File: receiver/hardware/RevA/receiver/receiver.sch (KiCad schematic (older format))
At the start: 1 part, among them U1 C8051F850-A-GU

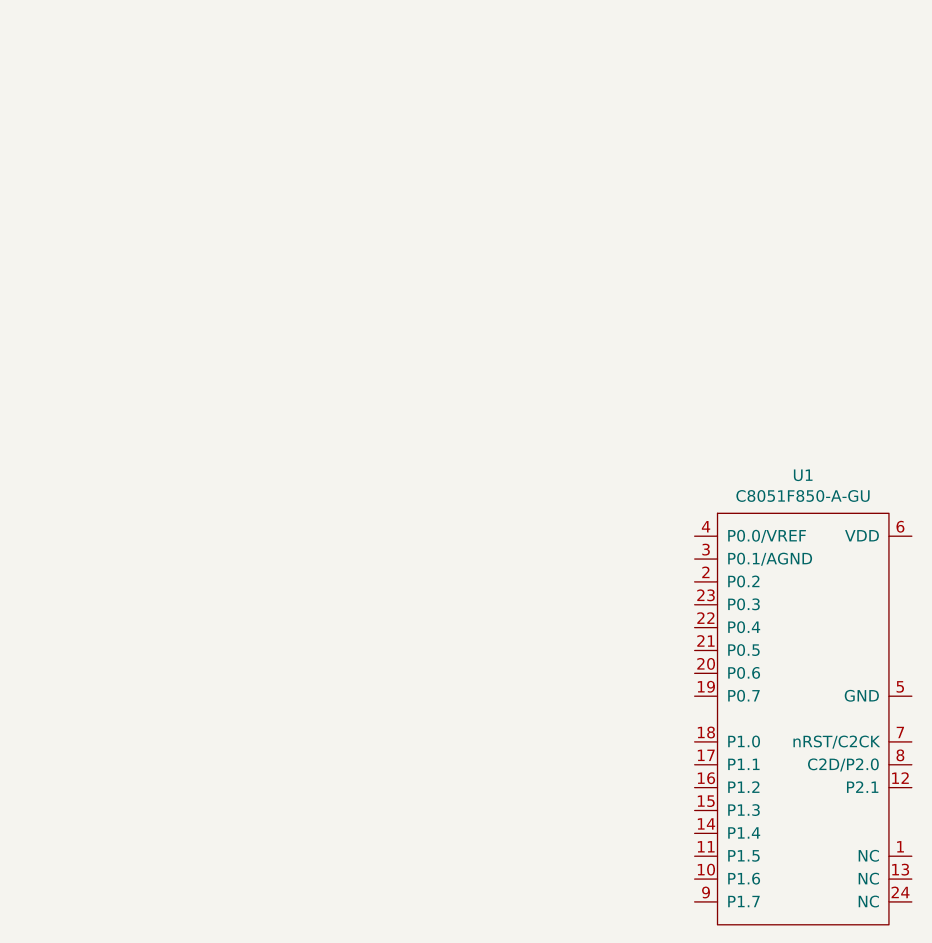
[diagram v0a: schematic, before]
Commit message: Added FT232RL
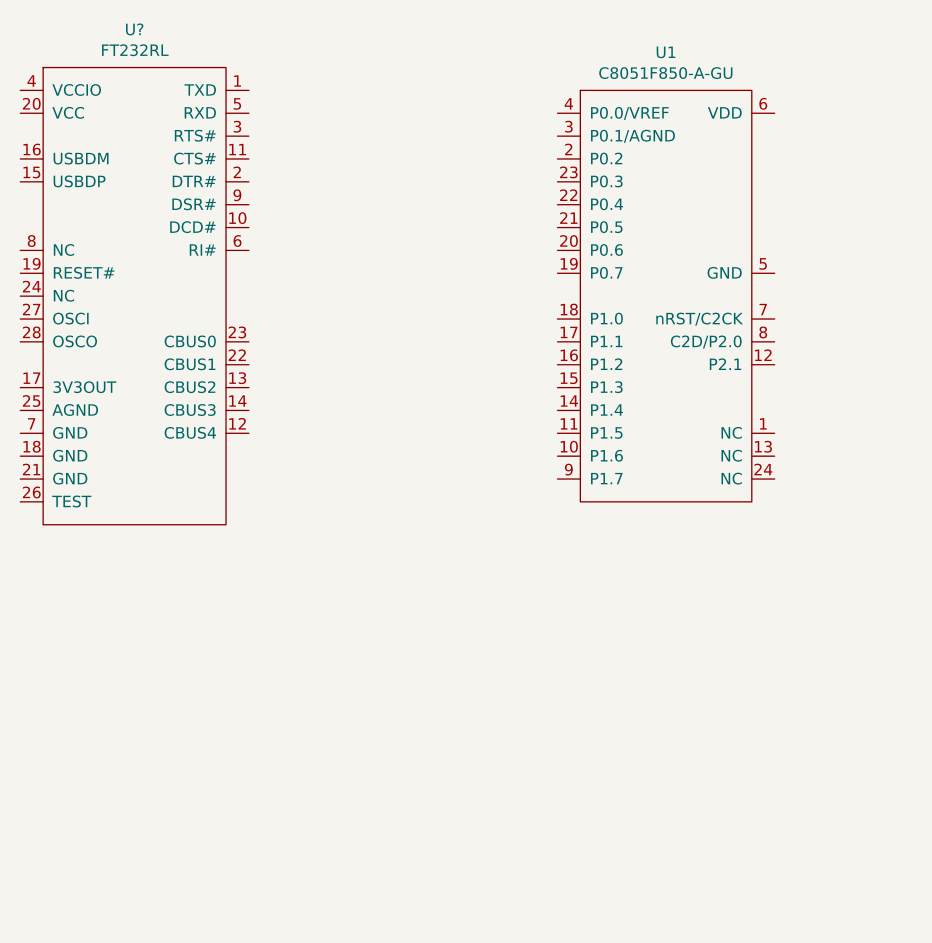
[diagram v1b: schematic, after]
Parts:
- added U?: FT232RL, symbol receiver:FT232RL
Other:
- moved on the sheet: U1
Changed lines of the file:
@@
 L receiver:C8051F850-A-GU U1
 U 1 1 61B9295A
-P 4550 4200
-F 0 "U1" H 5075 4365 50  0000 C CNN
-F 1 "C8051F850-A-GU" H 5075 4274 50  0000 C CNN
-F 2 "receiver:C8051F850-A-GU" H 4600 4100 50  0001 C CNN
-F 3 "" H 4600 4100 50  0001 C CNN
-	1    4550 4200
+P 3950 2350
+F 0 "U1" H 4475 2515 50  0000 C CNN
+F 1 "C8051F850-A-GU" H 4475 2424 50  0000 C CNN
+F 2 "receiver:C8051F850-A-GU" H 4000 2250 50  0001 C CNN
+F 3 "" H 4000 2250 50  0001 C CNN
+	1    3950 2350
 	1    0    0    -1
 $EndComp
+$Comp
+L receiver:FT232RL U?
+U 1 1 61BC06A2
+P 2650 2350
+F 0 "U?" H 2150 2615 50  0000 C CNN
+F 1 "FT232RL" H 2150 2524 50  0000 C CNN
+F 2 "" H 2650 2350 50  0001 C CNN
+F 3 "" H 2650 2350 50  0001 C CNN
+	1    2650 2350
+	1    0    0    -1
+$EndComp

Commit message: ftdi and usb
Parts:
- added J1: 48037-0001, receiver:48037-0001, symbol receiver:48037-0001
- U2: renamed from U?; footprint (none) -> receiver:FT232RL
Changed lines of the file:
@@
 $EndComp
 $Comp
-L receiver:FT232RL U?
+L receiver:FT232RL U2
 U 1 1 61BC06A2
 P 2650 2350
-F 0 "U?" H 2150 2615 50  0000 C CNN
+F 0 "U2" H 2150 2615 50  0000 C CNN
 F 1 "FT232RL" H 2150 2524 50  0000 C CNN
-F 2 "" H 2650 2350 50  0001 C CNN
+F 2 "receiver:FT232RL" H 2650 2350 50  0001 C CNN
 F 3 "" H 2650 2350 50  0001 C CNN
 	1    2650 2350
 	1    0    0    -1
 $EndComp
+$Comp
+L receiver:48037-0001 J1
+U 1 1 61BD1ABB
+P 900 2500
+F 0 "J1" H 858 2765 50  0000 C CNN
+F 1 "48037-0001" H 858 2674 50  0000 C CNN
+F 2 "receiver:48037-0001" H 900 2500 50  0001 C CNN
+F 3 "" H 900 2500 50  0001 C CNN
+	1    900  2500
+	1    0    0    -1
+$EndComp

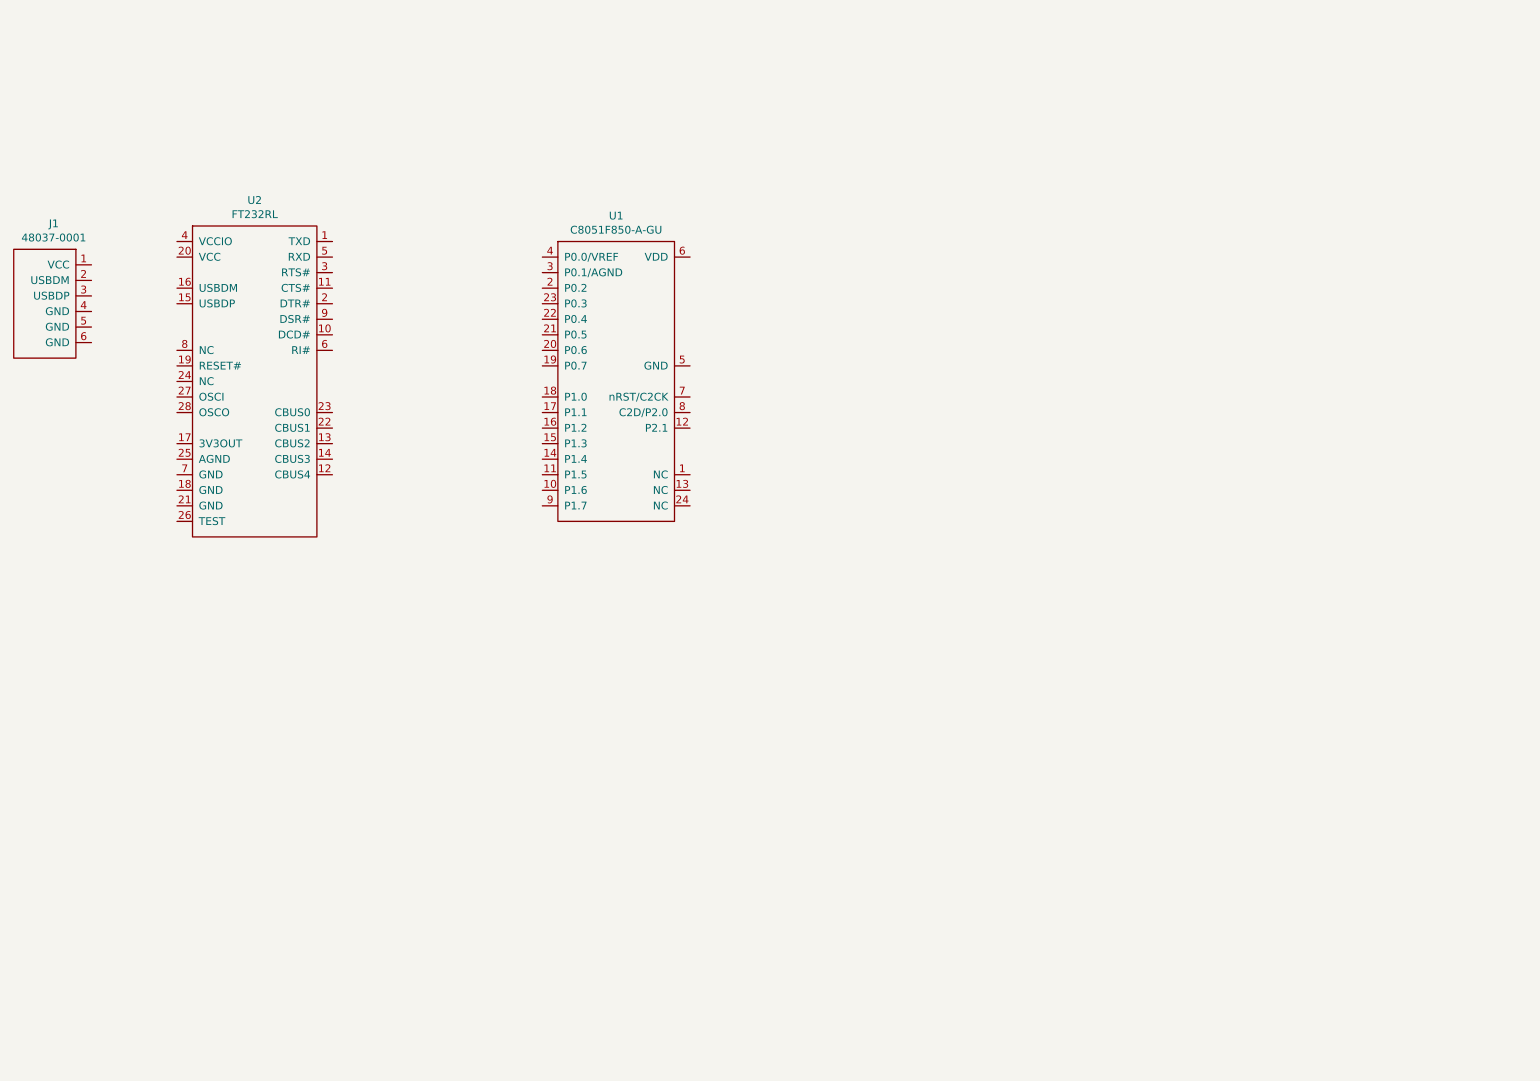
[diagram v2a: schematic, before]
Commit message: add connector
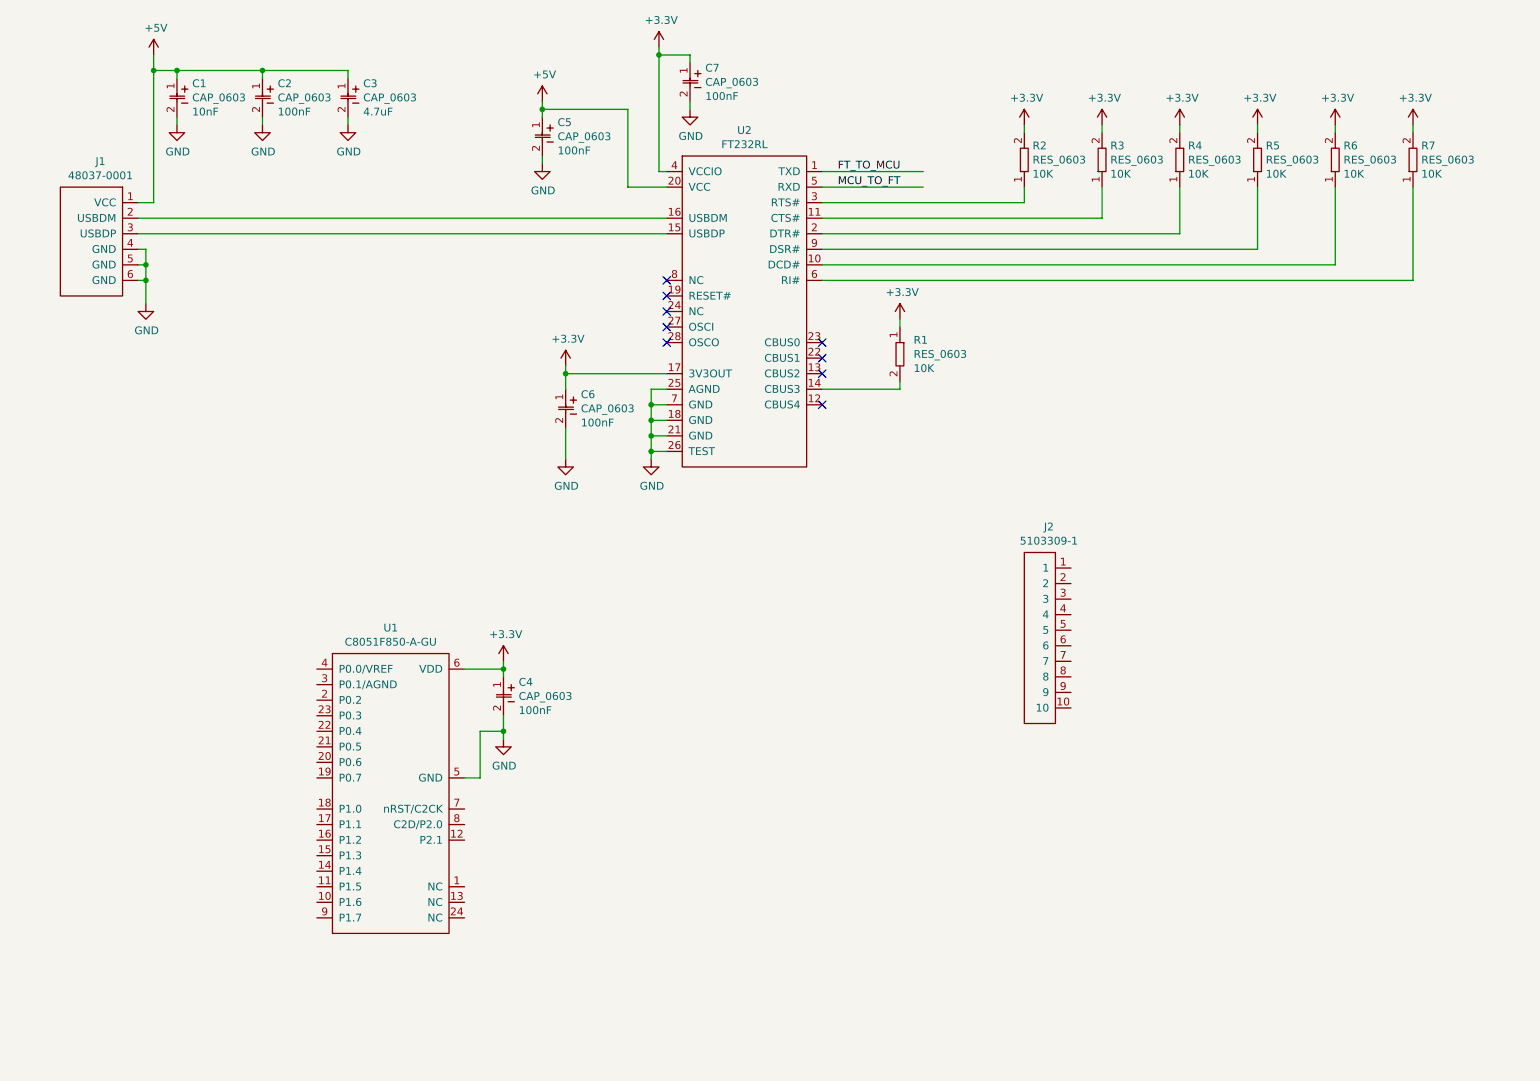
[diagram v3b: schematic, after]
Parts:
- added C1, C2, C3, C4, C5, C6, C7: CAP_0603, receiver:0603, symbol receiver:CAP_0603
- added J2: 5103309-1, receiver:5103309-1, symbol receiver:5103309-1
- added R1, R2, R3, R4, R5, R6, R7: RES_0603, receiver:0603, symbol receiver:RES_0603
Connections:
- net GND: now reaches U1.5 (GND)
- net GND: now also J1.4 (GND), J1.5 (GND), J1.6 (GND), U2.18 (GND), U2.21 (GND), U2.25 (AGND), U2.26 (TEST), U2.7 (GND), C1.2, C2.2, C3.2, C4.2, C5.2, C6.2, C7.2
- net +3V3: now reaches U1.6 (VDD)
- net +3V3: now also U2.17 (3V3OUT), U2.4 (VCCIO), C4.1, C6.1, C7.1, R1.1, R2.2, R3.2, R4.2, R5.2, R6.2, R7.2
- net FT_TO_MCU: now reaches U2.1 (TXD)
- net at U2.10 (DCD#): now also R6.1
- net at U2.11 (CTS#): now also R3.1
- net at U2.14 (CBUS3): now also R1.2
- net at U2.15 (USBDP): now also J1.3 (USBDP)
- net at U2.16 (USBDM): now also J1.2 (USBDM)
- net at U2.2 (DTR#): now also R4.1
- net +5V: now reaches U2.20 (VCC)
- net +5V: now also J1.1 (VCC), C1.1, C2.1, C3.1, C5.1
- net at U2.3 (RTS#): now also R2.1
- net MCU_TO_FT: now reaches U2.5 (RXD)
- net at U2.6 (RI#): now also R7.1
- net at U2.9 (DSR#): now also R5.1
- no-connect marks 0 -> 9
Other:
- moved on the sheet: J1, U1, U2

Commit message: connectors
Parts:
- added J3: 2212S-04SG-85, receiver:2212S-04SG-85, symbol receiver:2212S-04SG-85
- added R10, R8, R9: RES_0603, receiver:0603, symbol receiver:RES_0603
- added T00, T01, T02, T03, T04, T05, T06, T07, T10, T11, T12, T13, T14, T15, T16, T17, T21, T31, T32, T33, T40, T41, T42, T43, T44, T45, T46, T47, T48, T49, T50: TestPoints, receiver:TestPoint, symbol receiver:TestPoints
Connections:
- net labels added: RX, TCK_C2D, TDI_C2CK, TDO_C2D, TMS_C2CK, USB_PWR
- wire segments 77 -> 147
- no-connect marks 9 -> 14
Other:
- moved on the sheet: J2

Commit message: edge cuts
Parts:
- added C8: CAP_0603, receiver:0603, symbol receiver:CAP_0603
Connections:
- wire segments 147 -> 150
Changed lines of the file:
@@
 Connection ~ 8500 3550
 Wire Wire Line
-	8500 3550 8000 3550
+	8500 3550 8150 3550
 Wire Wire Line
 	9050 3400 9050 3550
@@
 	9050 3750 8850 3750
 Connection ~ 9050 3750
+$Comp
+L receiver:CAP_0603 C8
+U 1 1 61CBC808
+P 8150 3650
+F 0 "C8" H 8248 3616 50  0000 L CNN
+F 1 "CAP_0603" H 8248 3525 50  0000 L CNN
+F 2 "receiver:0603" H 8150 3650 50  0001 C CNN
+F 3 "" H 8150 3650 50  0001 C CNN
+F 4 "100nF" H 8248 3434 50  0000 L CNN "Capacitance"
+	1    8150 3650
+	1    0    0    -1
+$EndComp
+$Comp
+L power:GND #PWR?
+U 1 1 61CBDDB4
+P 8150 3950
+F 0 "#PWR?" H 8150 3700 50  0001 C CNN
+F 1 "GND" H 8155 3777 50  0000 C CNN
+F 2 "" H 8150 3950 50  0001 C CNN
+F 3 "" H 8150 3950 50  0001 C CNN
+	1    8150 3950
+	1    0    0    -1
+$EndComp
+Wire Wire Line
+	8150 3650 8150 3550
+Connection ~ 8150 3550
+Wire Wire Line
+	8150 3550 8000 3550
+Wire Wire Line
+	8150 3950 8150 3900
 $EndSCHEMATC

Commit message: finish layout
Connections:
- net labels added: VCC
- wire segments 150 -> 152
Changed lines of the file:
@@
 Wire Wire Line
 	8150 3950 8150 3900
+$Comp
+L power:VCC #PWR?
+U 1 1 61CA8A38
+P 7700 3450
+F 0 "#PWR?" H 7700 3300 50  0001 C CNN
+F 1 "VCC" H 7715 3623 50  0000 C CNN
+F 2 "" H 7700 3450 50  0001 C CNN
+F 3 "" H 7700 3450 50  0001 C CNN
+	1    7700 3450
+	1    0    0    -1
+$EndComp
+Wire Wire Line
+	8000 3550 7700 3550
+Wire Wire Line
+	7700 3550 7700 3450
+Connection ~ 8000 3550
 $EndSCHEMATC
